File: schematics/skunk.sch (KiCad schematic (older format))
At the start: 0 parts

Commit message: Added battery supply to schematic & gitignore
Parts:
- added BT?: 12V SLAB BAT1, symbol BATTERY
- added BT?: 12V SLAB BAT2, symbol BATTERY
- added P? (x2): CONN_BAT_1, symbol CONN_2
- added P? (x2): CONN_BAT_2, symbol CONN_2
- added P? (x2): CONN_ARD_POWER, symbol CONN_2
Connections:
- new net: BT?.1 (+), P?.2 (PM) (x2)
- new net: BT?.2 (-), P?.1 (P1) (x2)
- new net +12V: P?.1 (P1), P?.2 (PM), P?.2 (PM)
- new net +24V: P?.2 (PM)
- new net GND: P?.1 (P1), P?.1 (P1)
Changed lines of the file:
@@
-EESchema Schematic File Version 2  date 26/09/2012 14:06:01
+EESchema Schematic File Version 2  date 26/09/2012 21:02:12
 LIBS:power
 LIBS:device
@@
 LIBS:contrib
 LIBS:valves
-EELAYER 43  0
+LIBS:skunk-cache
+EELAYER 25  0
 EELAYER END
 $Descr A4 11700 8267
@@
 Comment4 ""
 $EndDescr
+$Comp
+L CONN_2 P?
+U 1 1 50635EC9
+P 1900 4050
+F 0 "P?" V 1850 4050 40  0000 C CNN
+F 1 "CONN_ARD_POWER" H 1750 4250 40  0000 C CNN
+	1    1900 4050
+	-1   0    0    1
+$EndComp
+Connection ~ 1650 2650
+Wire Wire Line
+	1250 3950 850  3950
+Wire Wire Line
+	850  3950 850  2900
+Wire Wire Line
+	1650 2900 850  2900
+Wire Wire Line
+	1650 2500 1650 2900
+Wire Wire Line
+	2700 2650 2450 2650
+Wire Wire Line
+	1650 2650 1900 2650
+Connection ~ 1650 2500
+Wire Wire Line
+	1300 2450 1300 2650
+Wire Wire Line
+	2050 1000 2050 1350
+Wire Wire Line
+	2050 1350 2250 1350
+Wire Wire Line
+	1300 1350 1100 1350
+Wire Wire Line
+	1100 1350 1100 1000
+Wire Wire Line
+	1700 1000 1700 1350
+Wire Wire Line
+	1700 1350 1500 1350
+Wire Wire Line
+	2450 1350 2650 1350
+Wire Wire Line
+	2650 1350 2650 1000
+Wire Wire Line
+	1500 2450 1500 2500
+Wire Wire Line
+	1500 2500 2250 2500
+Wire Wire Line
+	2250 2500 2250 2450
+Wire Wire Line
+	2450 2650 2450 2450
+Wire Wire Line
+	1300 2600 1450 2600
+Connection ~ 1300 2600
+Wire Wire Line
+	1450 2600 1450 2800
+Wire Wire Line
+	1450 2800 750  2800
+Wire Wire Line
+	750  2800 750  4150
+Wire Wire Line
+	750  4150 1250 4150
+$Comp
+L CONN_2 P?
+U 1 1 50635E8C
+P 1600 4050
+F 0 "P?" V 1550 4050 40  0000 C CNN
+F 1 "CONN_ARD_POWER" H 1450 4250 40  0000 C CNN
+	1    1600 4050
+	1    0    0    1
+$EndComp
+Text Label 2700 2650 2    60   ~ 0
++24V
+Text Label 1900 2650 2    60   ~ 0
++12V
+$Comp
+L GND #PWR?
+U 1 1 50635463
+P 1300 2650
+F 0 "#PWR?" H 1300 2650 30  0001 C CNN
+F 1 "GND" H 1300 2580 30  0001 C CNN
+	1    1300 2650
+	1    0    0    -1
+$EndComp
+$Comp
+L CONN_2 P?
+U 1 1 506353B8
+P 2350 2100
+F 0 "P?" V 2300 2100 40  0000 C CNN
+F 1 "CONN_BAT_2" V 2500 2100 40  0000 C CNN
+	1    2350 2100
+	0    -1   -1   0
+$EndComp
+$Comp
+L CONN_2 P?
+U 1 1 5063538D
+P 1400 2100
+F 0 "P?" V 1350 2100 40  0000 C CNN
+F 1 "CONN_BAT_1" V 1550 2100 40  0000 C CNN
+	1    1400 2100
+	0    -1   -1   0
+$EndComp
+$Comp
+L CONN_2 P?
+U 1 1 506352F3
+P 2350 1700
+F 0 "P?" V 2300 1700 40  0000 C CNN
+F 1 "CONN_BAT_2" V 2500 1700 40  0000 C CNN
+	1    2350 1700
+	0    -1   1    0
+$EndComp
+$Comp
+L CONN_2 P?
+U 1 1 506352C8
+P 1400 1700
+F 0 "P?" V 1350 1700 40  0000 C CNN
+F 1 "CONN_BAT_1" V 1550 1700 40  0000 C CNN
+	1    1400 1700
+	0    -1   1    0
+$EndComp
+$Comp
+L BATTERY BT?
+U 1 1 5063529E
+P 2350 1000
+F 0 "BT?" H 2350 1200 50  0000 C CNN
+F 1 "12V SLAB BAT2" H 2350 810 50  0000 C CNN
+	1    2350 1000
+	-1   0    0    -1
+$EndComp
+$Comp
+L BATTERY BT?
+U 1 1 5063529A
+P 1400 1000
+F 0 "BT?" H 1400 1200 50  0000 C CNN
+F 1 "12V SLAB BAT1" H 1400 810 50  0000 C CNN
+	1    1400 1000
+	-1   0    0    -1
+$EndComp
 $EndSCHEMATC

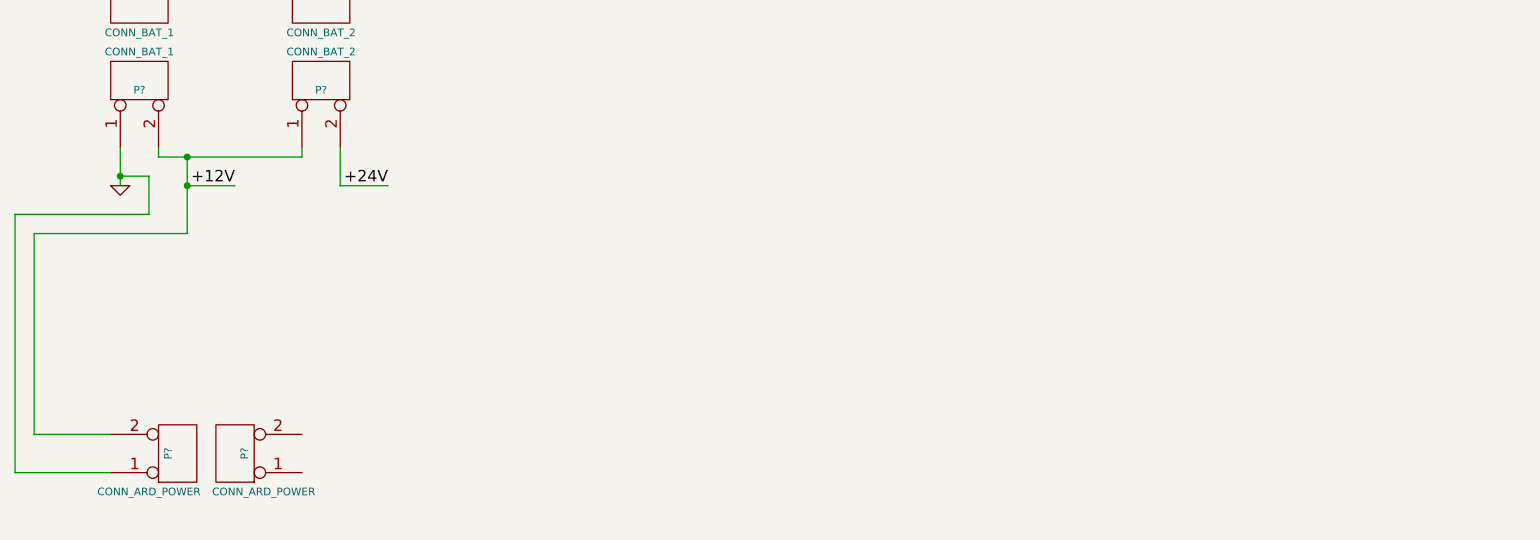
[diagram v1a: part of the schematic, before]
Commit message: Finished flowmeter wiring harness
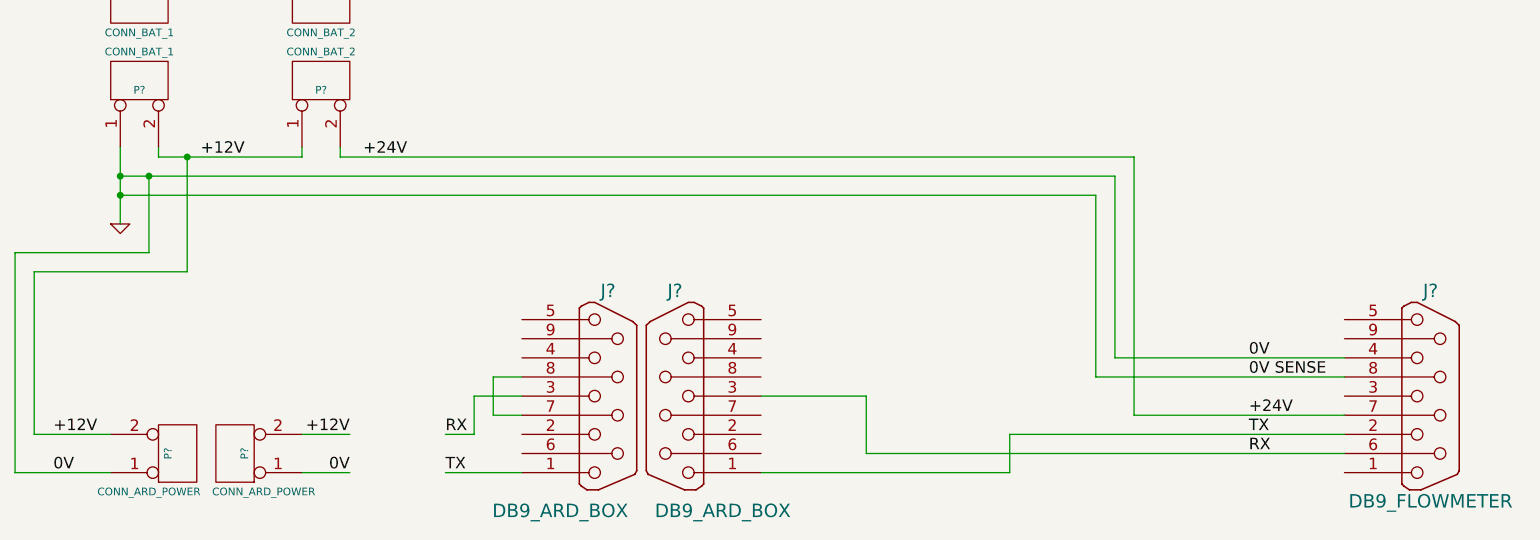
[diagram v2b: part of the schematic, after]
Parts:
- added J? (x2): DB9_ARD_BOX, symbol DB9
- added J?: DB9_FLOWMETER, symbol DB9
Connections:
- net +12V: now also P?.2 (PM)
- net +24V: now also J?.7 (P7)
- net GND: now also P?.1 (P1), J?.4, J?.8 (P8)
- new net: J?.7 (P7), J?.8 (P8)
- new net RX: J?.3, J?.3, J?.6 (P6)
- new net TX: J?.1, J?.1, J?.2
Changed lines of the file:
@@
-EESchema Schematic File Version 2  date 26/09/2012 21:02:12
+EESchema Schematic File Version 2  date 26/09/2012 21:33:07
 LIBS:power
 LIBS:device
@@
 Comment4 ""
 $EndDescr
+Wire Wire Line
+	3000 4150 3400 4150
+Wire Wire Line
+	2250 4150 2500 4150
+Connection ~ 1300 2700
+Wire Wire Line
+	1300 2850 1300 2450
+Wire Wire Line
+	1450 2600 1450 3000
+Wire Wire Line
+	1450 3000 750  3000
+Wire Wire Line
+	750  3000 750  4150
+Wire Wire Line
+	6400 3650 6400 2700
+Wire Wire Line
+	6400 3650 7700 3650
+Wire Wire Line
+	4650 3750 5200 3750
+Wire Wire Line
+	5200 3750 5200 4050
+Wire Wire Line
+	5200 4050 7700 4050
+Wire Wire Line
+	7700 3950 5950 3950
+Wire Wire Line
+	5950 3950 5950 4150
+Wire Wire Line
+	5950 4150 4650 4150
+Wire Wire Line
+	7700 3850 6600 3850
+Wire Wire Line
+	6600 3850 6600 2500
+Wire Wire Line
+	6600 2500 2450 2500
+Wire Wire Line
+	1250 3950 850  3950
+Connection ~ 1650 2500
+Wire Wire Line
+	2050 1000 2050 1350
+Wire Wire Line
+	2050 1350 2250 1350
+Wire Wire Line
+	1300 1350 1100 1350
+Wire Wire Line
+	1100 1350 1100 1000
+Wire Wire Line
+	1700 1000 1700 1350
+Wire Wire Line
+	1700 1350 1500 1350
+Wire Wire Line
+	2450 1350 2650 1350
+Wire Wire Line
+	2650 1350 2650 1000
+Wire Wire Line
+	1500 2450 1500 2500
+Wire Wire Line
+	1500 2500 2250 2500
+Wire Wire Line
+	2250 2500 2250 2450
+Connection ~ 1300 2600
+Wire Wire Line
+	750  4150 1250 4150
+Wire Wire Line
+	2450 2500 2450 2450
+Wire Wire Line
+	3400 3650 3250 3650
+Wire Wire Line
+	3250 3650 3250 3850
+Wire Wire Line
+	3250 3850 3400 3850
+Connection ~ 1450 2600
+Wire Wire Line
+	1300 2600 6500 2600
+Wire Wire Line
+	6500 2600 6500 3550
+Wire Wire Line
+	6500 3550 7700 3550
+Wire Wire Line
+	850  3950 850  3100
+Wire Wire Line
+	850  3100 1650 3100
+Wire Wire Line
+	1650 3100 1650 2500
+Wire Wire Line
+	6400 2700 1300 2700
+Wire Wire Line
+	2500 3950 2250 3950
+Wire Wire Line
+	3400 3750 3150 3750
+Wire Wire Line
+	3150 3750 3150 3950
+Wire Wire Line
+	3150 3950 3000 3950
+Text Label 2500 4150 2    60   ~ 0
+0V
+Text Label 2500 3950 2    60   ~ 0
++12V
+Text Label 7200 3650 0    60   ~ 0
+0V SENSE
+Text Label 7200 4050 0    60   ~ 0
+RX
+Text Label 7200 3850 0    60   ~ 0
++24V
+Text Label 7200 3950 0    60   ~ 0
+TX
+Text Label 7200 3550 0    60   ~ 0
+0V
+Text Label 950  4150 0    60   ~ 0
+0V
+Text Label 950  3950 0    60   ~ 0
++12V
+$Comp
+L DB9 J?
+U 1 1 506362ED
+P 8150 3750
+F 0 "J?" H 8150 4300 70  0000 C CNN
+F 1 "DB9_FLOWMETER" H 8150 3200 70  0000 C CNN
+	1    8150 3750
+	1    0    0    -1
+$EndComp
+Text Label 3000 3950 0    60   ~ 0
+RX
+Text Label 3000 4150 0    60   ~ 0
+TX
+$Comp
+L DB9 J?
+U 1 1 50636112
+P 3850 3750
+F 0 "J?" H 3850 4300 70  0000 C CNN
+F 1 "DB9_ARD_BOX" H 3600 3150 70  0000 C CNN
+	1    3850 3750
+	1    0    0    -1
+$EndComp
+$Comp
+L DB9 J?
+U 1 1 506360FD
+P 4200 3750
+F 0 "J?" H 4200 4300 70  0000 C CNN
+F 1 "DB9_ARD_BOX" H 3950 3150 70  0000 C CNN
+	1    4200 3750
+	-1   0    0    -1
+$EndComp
 $Comp
 L CONN_2 P?
@@
 	-1   0    0    1
 $EndComp
-Connection ~ 1650 2650
-Wire Wire Line
-	1250 3950 850  3950
-Wire Wire Line
-	850  3950 850  2900
-Wire Wire Line
-	1650 2900 850  2900
-Wire Wire Line
-	1650 2500 1650 2900
-Wire Wire Line
-	2700 2650 2450 2650
-Wire Wire Line
-	1650 2650 1900 2650
-Connection ~ 1650 2500
-Wire Wire Line
-	1300 2450 1300 2650
-Wire Wire Line
-	2050 1000 2050 1350
-Wire Wire Line
-	2050 1350 2250 1350
-Wire Wire Line
-	1300 1350 1100 1350
-Wire Wire Line
-	1100 1350 1100 1000
-Wire Wire Line
-	1700 1000 1700 1350
-Wire Wire Line
-	1700 1350 1500 1350
-Wire Wire Line
-	2450 1350 2650 1350
-Wire Wire Line
-	2650 1350 2650 1000
-Wire Wire Line
-	1500 2450 1500 2500
-Wire Wire Line
-	1500 2500 2250 2500
-Wire Wire Line
-	2250 2500 2250 2450
-Wire Wire Line
-	2450 2650 2450 2450
-Wire Wire Line
-	1300 2600 1450 2600
-Connection ~ 1300 2600
-Wire Wire Line
-	1450 2600 1450 2800
-Wire Wire Line
-	1450 2800 750  2800
-Wire Wire Line
-	750  2800 750  4150
-Wire Wire Line
-	750  4150 1250 4150
 $Comp
 L CONN_2 P?
@@
 	1    0    0    1
 $EndComp
-Text Label 2700 2650 2    60   ~ 0
+Text Label 2800 2500 2    60   ~ 0
 +24V
-Text Label 1900 2650 2    60   ~ 0
+Text Label 1950 2500 2    60   ~ 0
 +12V
 $Comp
 L GND #PWR?
 U 1 1 50635463
-P 1300 2650
-F 0 "#PWR?" H 1300 2650 30  0001 C CNN
-F 1 "GND" H 1300 2580 30  0001 C CNN
-	1    1300 2650
+P 1300 2850
+F 0 "#PWR?" H 1300 2850 30  0001 C CNN
+F 1 "GND" H 1300 2780 30  0001 C CNN
+	1    1300 2850
 	1    0    0    -1
 $EndComp

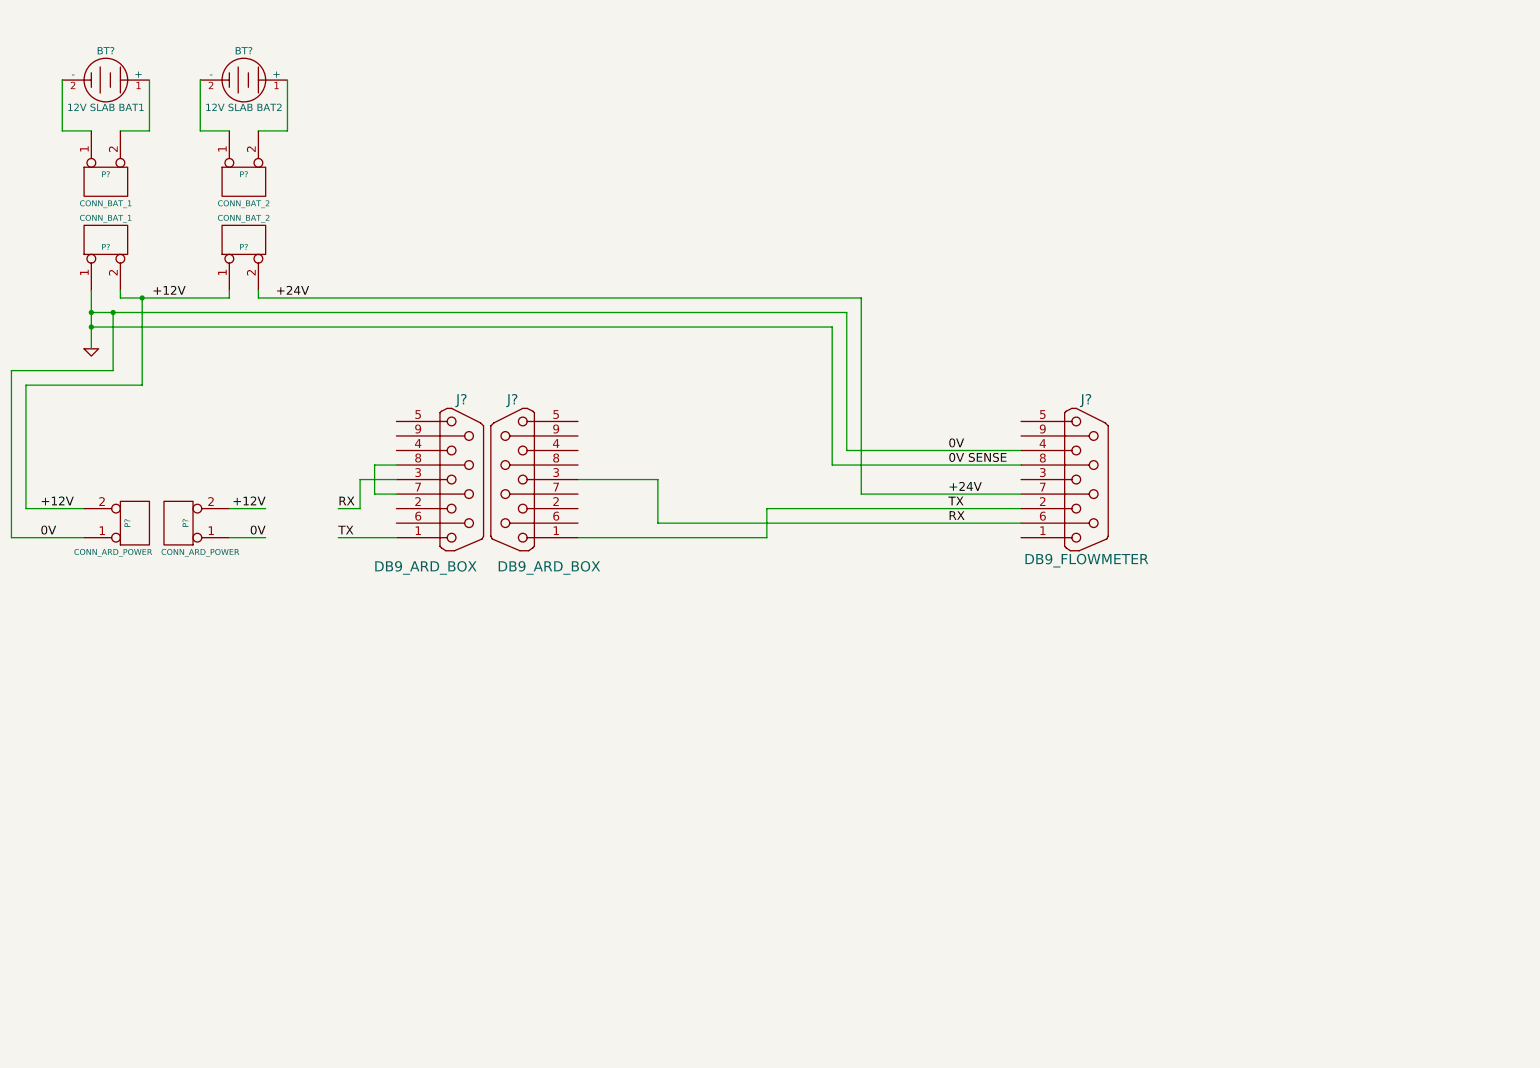
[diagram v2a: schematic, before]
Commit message: Fixed flowmeter wiring harness, added ARD box
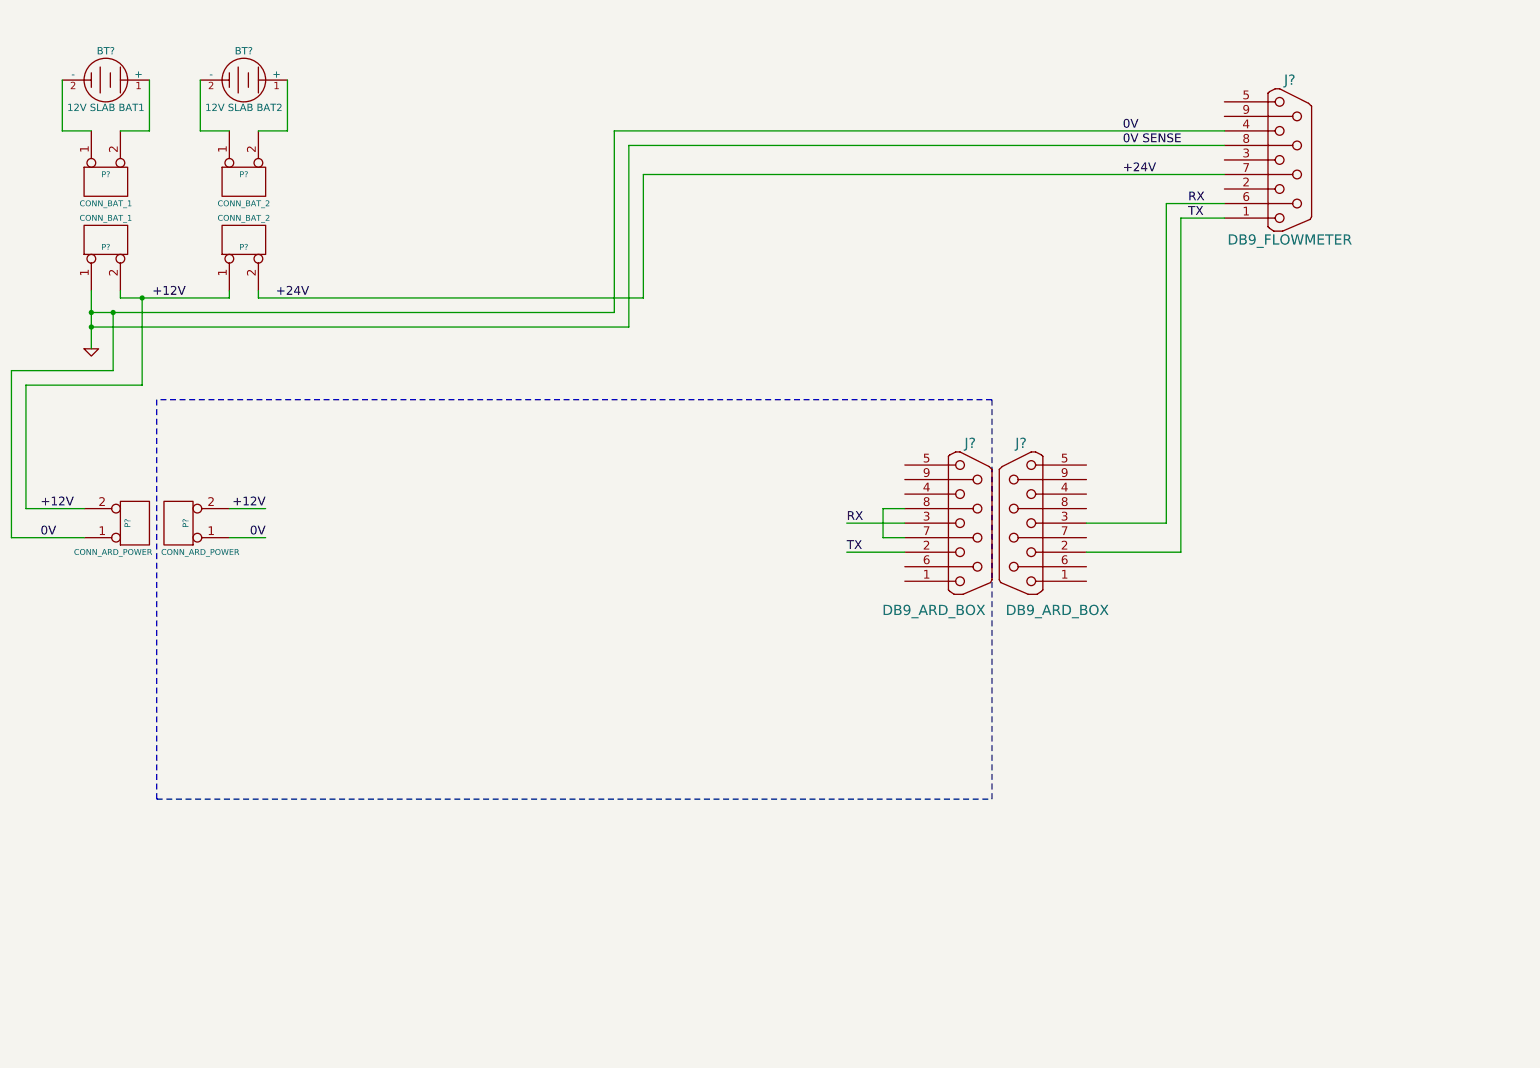
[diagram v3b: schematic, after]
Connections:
- net TX: now also J?.1, J?.2, J?.2; no longer J?.1, J?.1, J?.2
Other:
- moved on the sheet: J?
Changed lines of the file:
@@
-EESchema Schematic File Version 2  date 26/09/2012 21:33:07
+EESchema Schematic File Version 2  date 26/09/2012 21:43:37
 LIBS:power
 LIBS:device
@@
 Comment4 ""
 $EndDescr
+Wire Notes Line
+	1750 5950 1750 3200
+Wire Notes Line
+	1750 5950 7500 5950
+Wire Notes Line
+	7500 5950 7500 3200
+Wire Notes Line
+	7500 3200 1750 3200
 Wire Wire Line
-	3000 4150 3400 4150
+	9100 1850 8700 1850
+Wire Wire Line
+	8700 1850 8700 4050
+Wire Wire Line
+	6900 4250 6500 4250
+Wire Wire Line
+	9100 1450 5000 1450
+Wire Wire Line
+	5000 1450 5000 2700
+Wire Wire Line
+	5000 2700 1300 2700
 Wire Wire Line
 	2250 4150 2500 4150
@@
 	750  3000 750  4150
 Wire Wire Line
-	6400 3650 6400 2700
-Wire Wire Line
-	6400 3650 7700 3650
-Wire Wire Line
-	4650 3750 5200 3750
-Wire Wire Line
-	5200 3750 5200 4050
-Wire Wire Line
-	5200 4050 7700 4050
-Wire Wire Line
-	7700 3950 5950 3950
-Wire Wire Line
-	5950 3950 5950 4150
-Wire Wire Line
-	5950 4150 4650 4150
-Wire Wire Line
-	7700 3850 6600 3850
-Wire Wire Line
-	6600 3850 6600 2500
-Wire Wire Line
-	6600 2500 2450 2500
+	8700 4050 8150 4050
 Wire Wire Line
 	1250 3950 850  3950
@@
 	750  4150 1250 4150
 Wire Wire Line
-	2450 2500 2450 2450
+	2450 2450 2450 2500
 Wire Wire Line
-	3400 3650 3250 3650
+	6900 3950 6750 3950
 Wire Wire Line
-	3250 3650 3250 3850
+	6750 3950 6750 4150
 Wire Wire Line
-	3250 3850 3400 3850
+	6750 4150 6900 4150
 Connection ~ 1450 2600
-Wire Wire Line
-	1300 2600 6500 2600
-Wire Wire Line
-	6500 2600 6500 3550
-Wire Wire Line
-	6500 3550 7700 3550
 Wire Wire Line
 	850  3950 850  3100
@@
 	1650 3100 1650 2500
 Wire Wire Line
-	6400 2700 1300 2700
-Wire Wire Line
 	2500 3950 2250 3950
 Wire Wire Line
-	3400 3750 3150 3750
+	1300 2600 4900 2600
 Wire Wire Line
-	3150 3750 3150 3950
+	4900 2600 4900 1350
 Wire Wire Line
-	3150 3950 3000 3950
+	4900 1350 9100 1350
+Wire Wire Line
+	2450 2500 5100 2500
+Wire Wire Line
+	5100 2500 5100 1650
+Wire Wire Line
+	5100 1650 9100 1650
+Wire Wire Line
+	6500 4050 6900 4050
+Wire Wire Line
+	8150 4250 8800 4250
+Wire Wire Line
+	8800 4250 8800 1950
+Wire Wire Line
+	8800 1950 9100 1950
+Text Label 6500 4050 0    60   ~ 0
+RX
 Text Label 2500 4150 2    60   ~ 0
 0V
 Text Label 2500 3950 2    60   ~ 0
 +12V
-Text Label 7200 3650 0    60   ~ 0
+Text Label 8400 1450 0    60   ~ 0
 0V SENSE
-Text Label 7200 4050 0    60   ~ 0
+Text Label 8850 1850 0    60   ~ 0
 RX
-Text Label 7200 3850 0    60   ~ 0
+Text Label 8400 1650 0    60   ~ 0
 +24V
-Text Label 7200 3950 0    60   ~ 0
+Text Label 8850 1950 0    60   ~ 0
 TX
-Text Label 7200 3550 0    60   ~ 0
+Text Label 8400 1350 0    60   ~ 0
 0V
 Text Label 950  4150 0    60   ~ 0
@@
 L DB9 J?
 U 1 1 506362ED
-P 8150 3750
-F 0 "J?" H 8150 4300 70  0000 C CNN
-F 1 "DB9_FLOWMETER" H 8150 3200 70  0000 C CNN
-	1    8150 3750
+P 9550 1550
+F 0 "J?" H 9550 2100 70  0000 C CNN
+F 1 "DB9_FLOWMETER" H 9550 1000 70  0000 C CNN
+	1    9550 1550
 	1    0    0    -1
 $EndComp
-Text Label 3000 3950 0    60   ~ 0
-RX
-Text Label 3000 4150 0    60   ~ 0
+Text Label 6500 4250 0    60   ~ 0
 TX
 $Comp
 L DB9 J?
 U 1 1 50636112
-P 3850 3750
-F 0 "J?" H 3850 4300 70  0000 C CNN
-F 1 "DB9_ARD_BOX" H 3600 3150 70  0000 C CNN
-	1    3850 3750
+P 7350 4050
+F 0 "J?" H 7350 4600 70  0000 C CNN
+F 1 "DB9_ARD_BOX" H 7100 3450 70  0000 C CNN
+	1    7350 4050
 	1    0    0    -1
 $EndComp
@@
 L DB9 J?
 U 1 1 506360FD
-P 4200 3750
-F 0 "J?" H 4200 4300 70  0000 C CNN
-F 1 "DB9_ARD_BOX" H 3950 3150 70  0000 C CNN
-	1    4200 3750
+P 7700 4050
+F 0 "J?" H 7700 4600 70  0000 C CNN
+F 1 "DB9_ARD_BOX" H 7450 3450 70  0000 C CNN
+	1    7700 4050
 	-1   0    0    -1
 $EndComp
